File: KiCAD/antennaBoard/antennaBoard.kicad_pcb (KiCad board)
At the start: 2 copper layers, 100 x 100 mm, 1 part

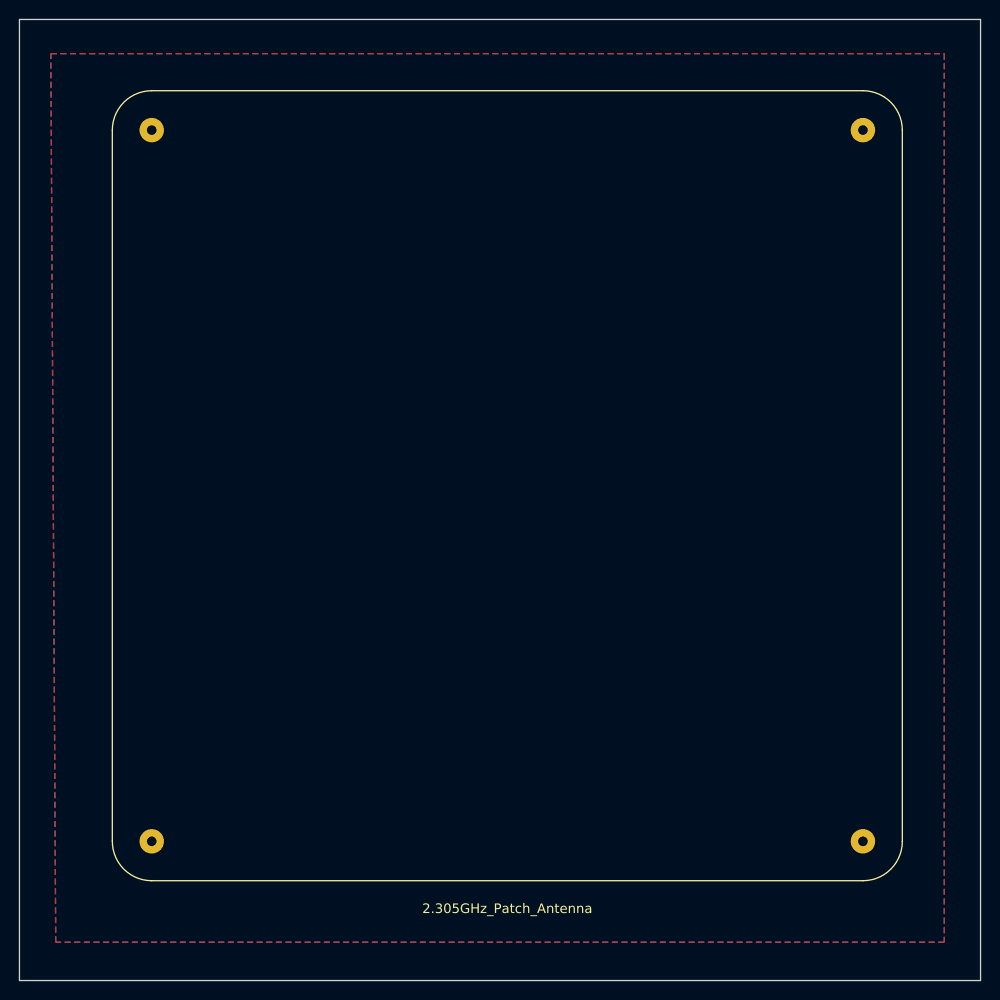
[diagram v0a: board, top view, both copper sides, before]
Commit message: Add coax
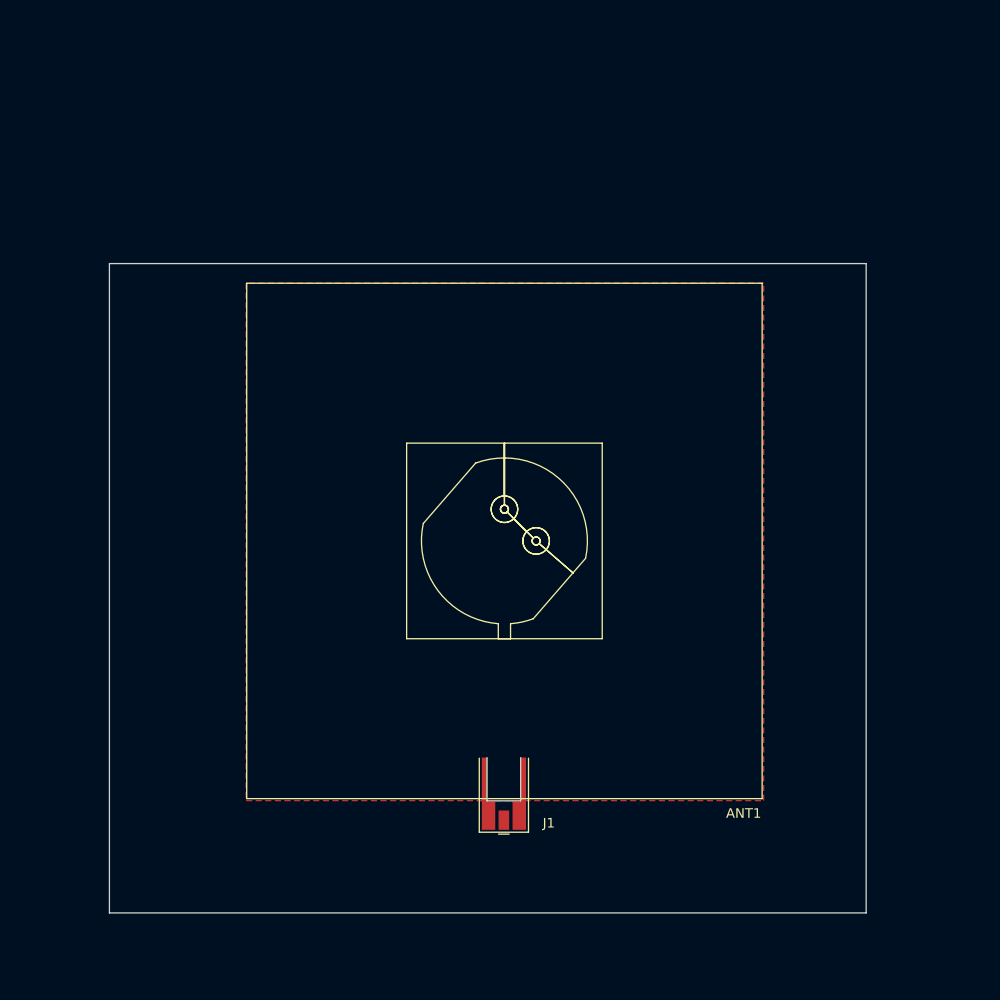
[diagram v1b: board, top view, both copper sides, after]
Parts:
- removed R: 2.305GHz_Patch_Antenna, RF_Antenna:InspireflyPatchAntenna
- added ANT1: 2.305GHz Patch, Inspirefly:CircularPatchAntenna, F.Cu at (158.0, 98.6)
- added J1: Conn_Coaxial, Connector_Coaxial:MMCX_Molex_73415-0961_Horizontal_0.8mm-PCB, F.Cu at (157.9, 125.3)
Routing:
- added copper zone on F.Cu, net Net-(ANT1-A)
- removed copper zone on B.Cu, net (none)
- removed copper zone on F.Cu, net (none)
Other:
- board size 100 x 100 mm -> 78.7 x 67.6 mm
- copper layers 2 -> 4

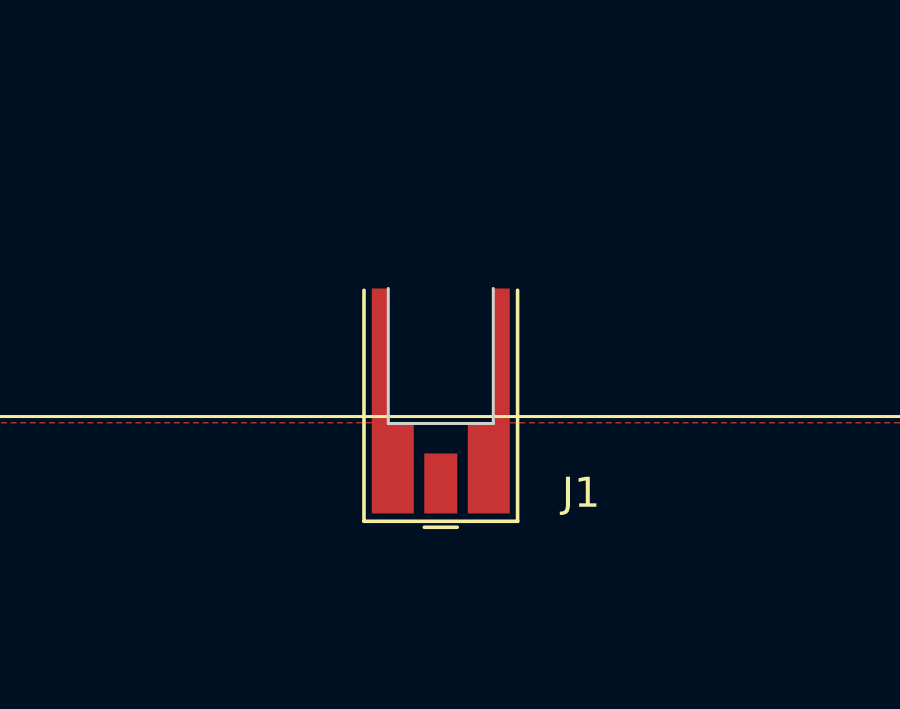
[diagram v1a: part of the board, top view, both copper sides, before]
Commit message: Add coax
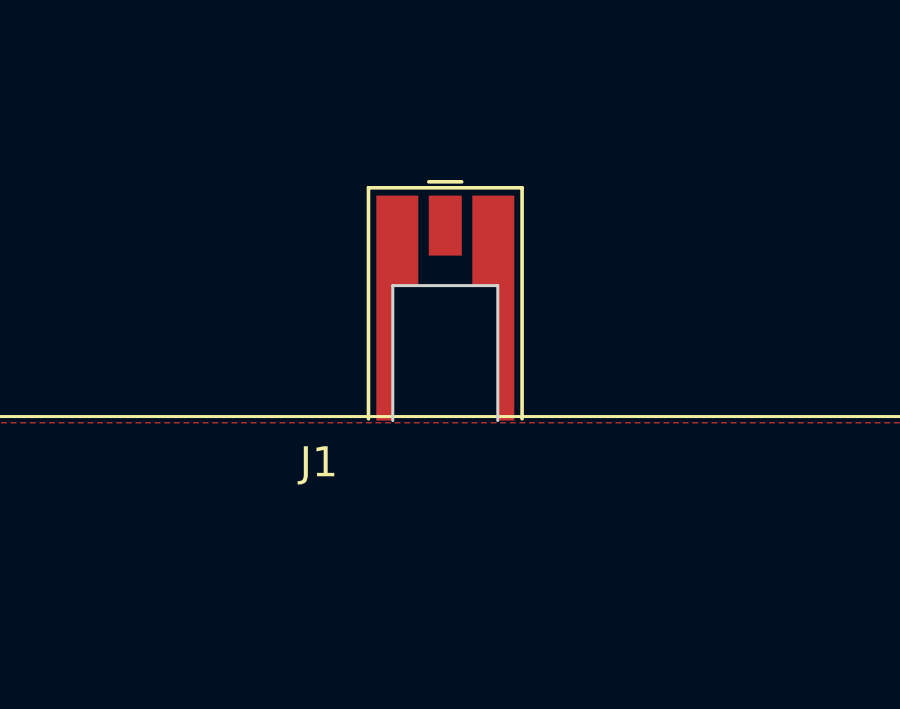
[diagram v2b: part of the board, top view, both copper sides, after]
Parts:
- moved J1 3.10 mm to (158.0, 122.2), turned to 90 degrees
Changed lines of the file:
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@@
 	(footprint "Connector_Coaxial:MMCX_Molex_73415-0961_Horizontal_0.8mm-PCB"
 		(layer "F.Cu")
-		(at 157.884 125.258 -90)
+		(at 158.034 122.162 90)
 		(descr "Molex MMCX Horizontal Coaxial https://www.molex.com/pdm_docs/sd/734150961_sd.pdf")
 		(tags "Molex MMCX Horizontal Coaxial")
 		(property "Reference" "J1"
-			(at 3.0628 -4.676 180)
+			(at -5.1428 -4.2116 0)
 			(layer "F.SilkS")
 			(effects
@@
 		)
 		(property "Value" "Conn_Coaxial"
-			(at 3.1644 8.532 180)
+			(at -5.0412 8.082 0)
 			(layer "F.Fab")
 			(effects
@@
 		)
 		(property "Datasheet" ""
-			(at 0 0 270)
+			(at 0 0 90)
 			(unlocked yes)
 			(layer "F.Fab")
@@
 		)
 		(property "Description" "coaxial connector (BNC, SMA, SMB, SMC, Cinch/RCA, LEMO, ...)"
-			(at 0 0 270)
+			(at 0 0 90)
 			(unlocked yes)
 			(layer "F.Fab")
@@
 		(duplicate_pad_numbers_are_jumpers no)
 		(fp_line
+			(start -3.69 -2.56)
+			(end 4.01 -2.56)
+			(stroke
+				(width 0.12)
+				(type solid)
+			)
+			(layer "F.SilkS")
+		)
+		(fp_line
+			(start 4.21 -0.55)
+			(end 4.21 0.55)
+			(stroke
+				(width 0.12)
+				(type solid)
+			)
+			(layer "F.SilkS")
+		)
+		(fp_line
+			(start 4.01 2.56)
+			(end 4.01 -2.56)
+			(stroke
+				(width 0.12)
+				(type solid)
+			)
+			(layer "F.SilkS")
+		)
+		(fp_line
 			(start -3.69 2.56)
 			(end 4.01 2.56)
@@
 		)
 		(fp_line
-			(start 4.01 2.56)
-			(end 4.01 -2.56)
-			(stroke
-				(width 0.12)
-				(type solid)
-			)
-			(layer "F.SilkS")
-		)
-		(fp_line
-			(start 4.21 -0.55)
-			(end 4.21 0.55)
-			(stroke
-				(width 0.12)
-				(type solid)
-			)
-			(layer "F.SilkS")
-		)
-		(fp_line
-			(start -3.69 -2.56)
-			(end 4.01 -2.56)
-			(stroke
-				(width 0.12)
-				(type solid)
-			)
-			(layer "F.SilkS")
-		)
-		(fp_line
 			(start -3.75 1.75)
 			(end -3.75 -1.75)
@@
 		)
 		(fp_line
+			(start 0.75 -1.75)
+			(end -3.75 -1.75)
+			(stroke
+				(width 0.1)
+				(type solid)
+			)
+			(layer "Edge.Cuts")
+		)
+		(fp_line
+			(start 0.75 1.75)
+			(end 0.75 -1.75)
+			(stroke
+				(width 0.1)
+				(type solid)
+			)
+			(layer "Edge.Cuts")
+		)
+		(fp_line
 			(start -3.75 1.75)
 			(end 0.75 1.75)
@@
 		)
 		(fp_line
-			(start 0.75 1.75)
-			(end 0.75 -1.75)
-			(stroke
-				(width 0.1)
-				(type solid)
-			)
-			(layer "Edge.Cuts")
-		)
-		(fp_line
-			(start 0.75 -1.75)
-			(end -3.75 -1.75)
-			(stroke
-				(width 0.1)
-				(type solid)
-			)
-			(layer "Edge.Cuts")
+			(start 4.25 -2.8)
+			(end 4.25 2.8)
+			(stroke
+				(width 0.05)
+				(type solid)
+			)
+			(layer "F.CrtYd")
+		)
+		(fp_line
+			(start -4.25 -2.8)
+			(end 4.25 -2.8)
+			(stroke
+				(width 0.05)
+				(type solid)
+			)
+			(layer "F.CrtYd")
+		)
+		(fp_line
+			(start -4.25 -2.8)
+			(end -4.25 2.8)
+			(stroke
+				(width 0.05)
+				(type solid)
+			)
+			(layer "F.CrtYd")
 		)
 		(fp_line
@@
 		)
 		(fp_line
-			(start -4.25 -2.8)
-			(end -4.25 2.8)
-			(stroke
-				(width 0.05)
-				(type solid)
-			)
-			(layer "F.CrtYd")
-		)
-		(fp_line
-			(start -4.25 -2.8)
-			(end 4.25 -2.8)
-			(stroke
-				(width 0.05)
-				(type solid)
-			)
-			(layer "F.CrtYd")
-		)
-		(fp_line
-			(start 4.25 -2.8)
-			(end 4.25 2.8)
-			(stroke
-				(width 0.05)
-				(type solid)
-			)
-			(layer "F.CrtYd")
+			(start -3.75 -2.25)
+			(end 3.68 -2.25)
+			(stroke
+				(width 0.1)
+				(type solid)
+			)
+			(layer "F.Fab")
+		)
+		(fp_line
+			(start -3.75 -2.25)
+			(end -3.75 2.25)
+			(stroke
+				(width 0.1)
+				(type solid)
+			)
+			(layer "F.Fab")
+		)
+		(fp_line
+			(start 3.68 -0.5)
+			(end 3.68 -2.25)
+			(stroke
+				(width 0.1)
+				(type solid)
+			)
+			(layer "F.Fab")
+		)
+		(fp_line
+			(start 3.18 0)
+			(end 3.68 -0.5)
+			(stroke
+				(width 0.1)
+				(type solid)
+			)
+			(layer "F.Fab")
+		)
+		(fp_line
+			(start 3.18 0)
+			(end 3.68 0.5)
+			(stroke
+				(width 0.1)
+				(type solid)
+			)
+			(layer "F.Fab")
+		)
+		(fp_line
+			(start 3.68 2.25)
+			(end 3.68 0.5)
+			(stroke
+				(width 0.1)
+				(type solid)
+			)
+			(layer "F.Fab")
 		)
 		(fp_line
 			(start -3.75 2.25)
 			(end 3.68 2.25)
-			(stroke
-				(width 0.1)
-				(type solid)
-			)
-			(layer "F.Fab")
-		)
-		(fp_line
-			(start 3.68 2.25)
-			(end 3.68 0.5)
-			(stroke
-				(width 0.1)
-				(type solid)
-			)
-			(layer "F.Fab")
-		)
-		(fp_line
-			(start 3.18 0)
-			(end 3.68 0.5)
-			(stroke
-				(width 0.1)
-				(type solid)
-			)
-			(layer "F.Fab")
-		)
-		(fp_line
-			(start 3.18 0)
-			(end 3.68 -0.5)
-			(stroke
-				(width 0.1)
-				(type solid)
-			)
-			(layer "F.Fab")
-		)
-		(fp_line
-			(start 3.68 -0.5)
-			(end 3.68 -2.25)
-			(stroke
-				(width 0.1)
-				(type solid)
-			)
-			(layer "F.Fab")
-		)
-		(fp_line
-			(start -3.75 -2.25)
-			(end -3.75 2.25)
-			(stroke
-				(width 0.1)
-				(type solid)
-			)
-			(layer "F.Fab")
-		)
-		(fp_line
-			(start -3.75 -2.25)
-			(end 3.68 -2.25)
 			(stroke
 				(width 0.1)
@@
 		)
 		(fp_text user "${REFERENCE}"
-			(at 3.0628 -4.676 180)
+			(at -5.1428 -4.2116 0)
 			(layer "F.Fab")
 			(effects
@@
 		)
 		(pad "1" smd rect
-			(at 2.75 0 270)
+			(at 2.75 0 90)
 			(size 2 1.1)
 			(layers "F.Cu" "F.Mask" "F.Paste")
@@
 		)
 		(pad "2" smd custom
-			(at 2.25 -1.6 270)
+			(at 2.25 -1.6 90)
 			(size 3 1.4)
 			(layers "F.Cu" "F.Mask" "F.Paste")
@@
 		)
 		(pad "2" smd custom
-			(at 2.25 1.6 270)
+			(at 2.25 1.6 90)
 			(size 3 1.4)
 			(layers "F.Cu" "F.Mask" "F.Paste")

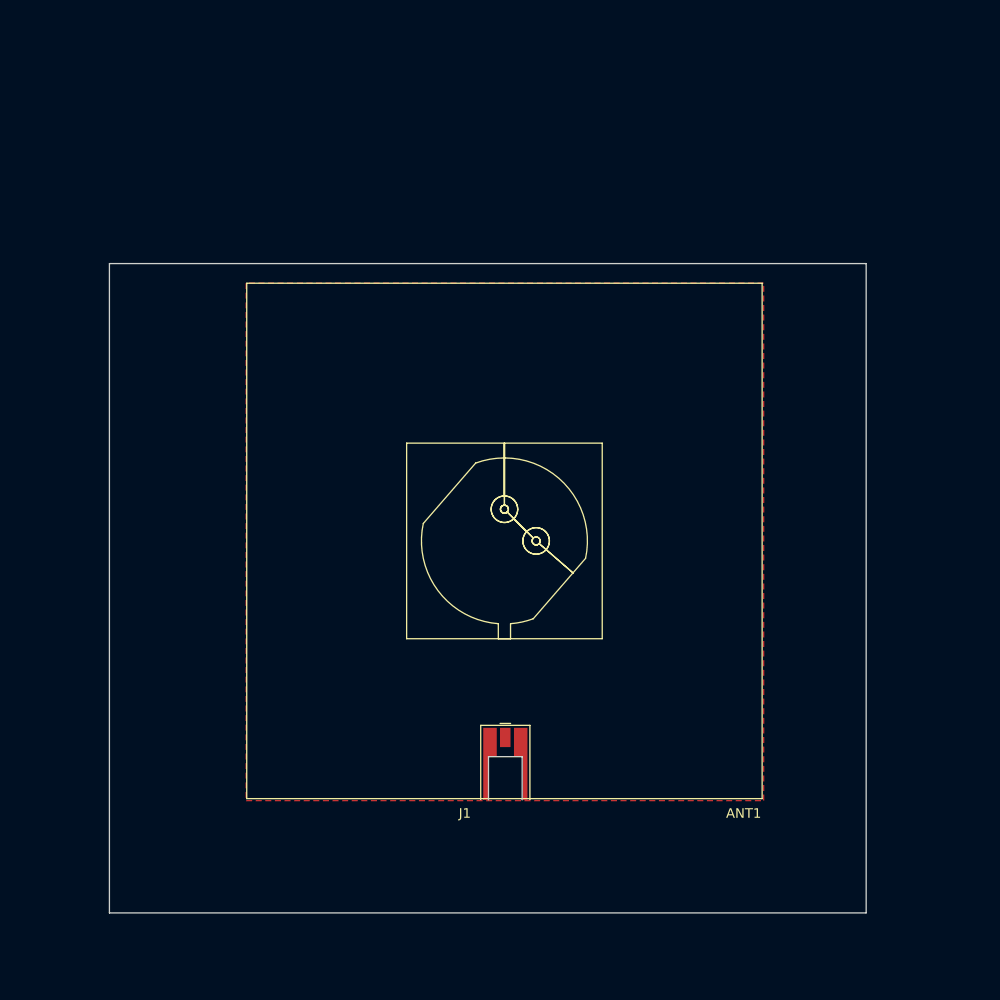
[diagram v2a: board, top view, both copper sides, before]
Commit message: Impl 2 coax feed
Use external power divider: APS-02-WBM-LP-DF-CC
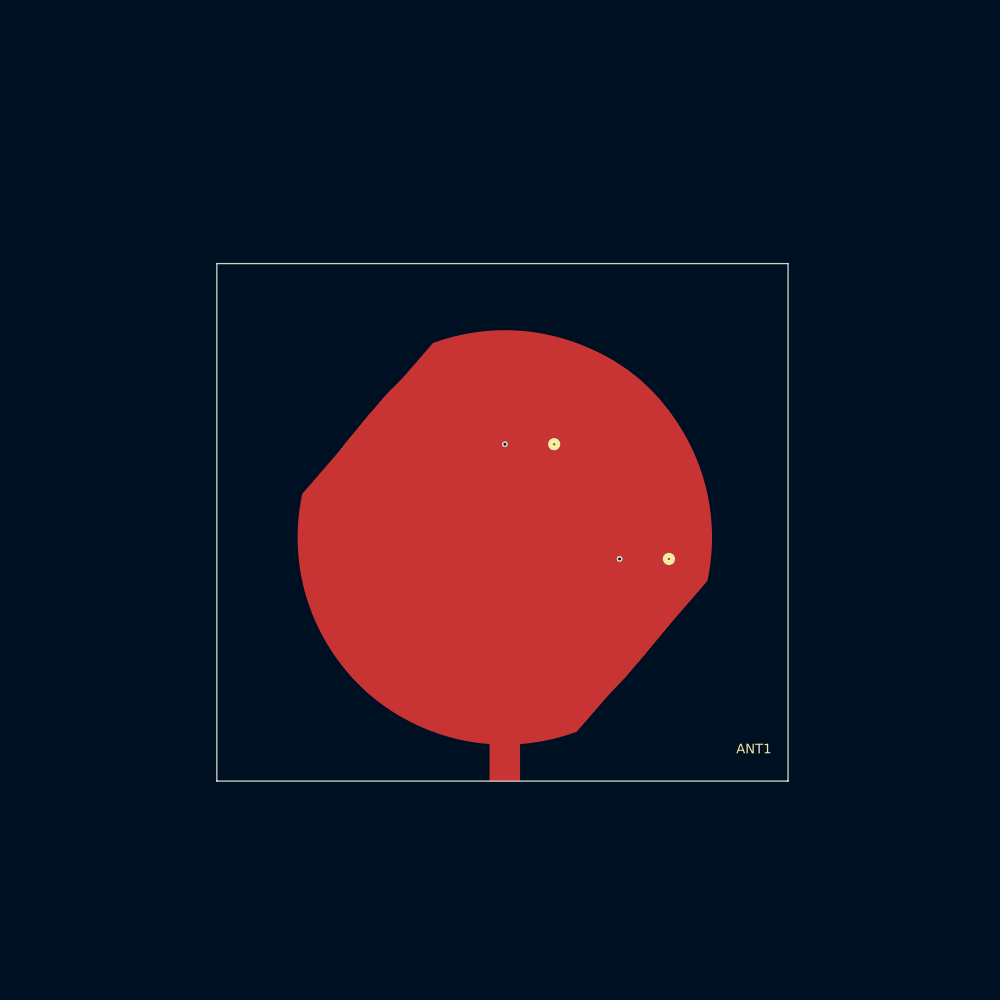
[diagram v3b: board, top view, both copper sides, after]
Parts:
- added J3: Conn_Coaxial, Inspirefly:CONN_732511350_MOL, B.Cu at (158.0, 88.9)
- J1: footprint Connector_Coaxial:MMCX_Molex_73415-0961_Horizontal_0.8mm-PCB -> Inspirefly:CONN_732511350_MOL; moved to B.Cu
- moved J1 24.4 mm to (169.9, 100.8), turned to 180 degrees
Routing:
- net GND: track 0.00 -> 16.9 mm
- net Net-(ANT1-A): vias 0 -> 2
- removed copper zone on F.Cu, net Net-(ANT1-A)
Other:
- board size 78.7 x 67.6 mm -> 59.4 x 53.8 mm
